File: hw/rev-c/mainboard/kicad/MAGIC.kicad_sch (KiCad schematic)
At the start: 16 parts, among them U7 SN74LVC4245APWR, U8 SN74LVC4245APWR, U9 SN74LVC4245APWR

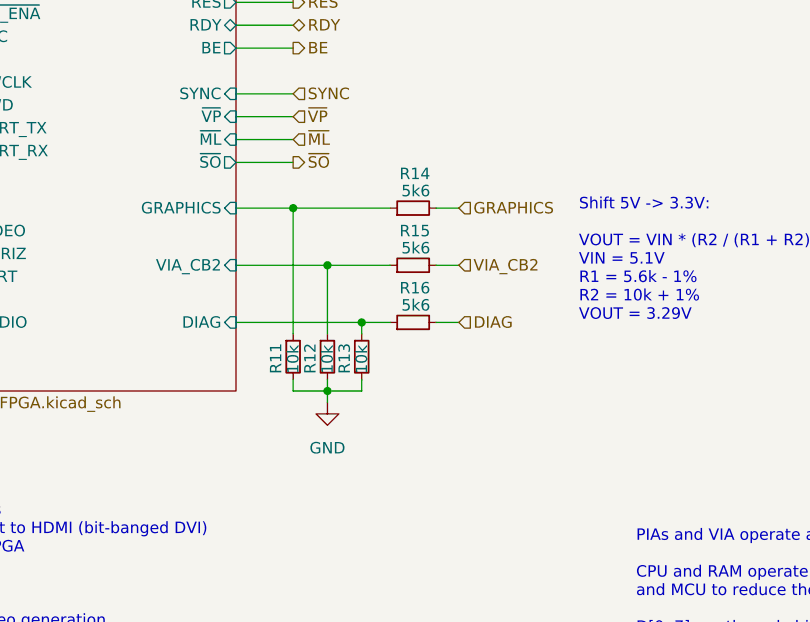
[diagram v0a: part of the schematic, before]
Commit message: hw: fix wire/grid violations in schematic
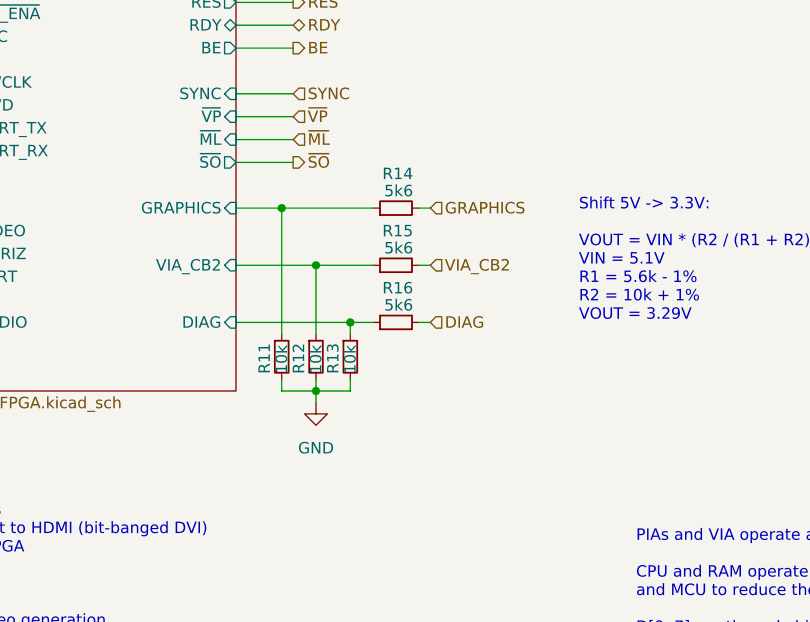
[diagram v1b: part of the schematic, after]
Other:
- moved on the sheet: R11, R12, R13, R14, R15, R16

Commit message: hw: more symbol updates
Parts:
- U7, U8, U9: symbol Mainboard-rescue:SN74LVC8T245-PET -> EconoPET:SN74LVC8T245
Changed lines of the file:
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@@
 	)
 	(symbol
-		(lib_id "Mainboard-rescue:SN74LVC8T245-PET")
+		(lib_id "EconoPET:SN74LVC8T245")
 		(at 220.98 44.45 0)
 		(mirror y)
@@
 	)
 	(symbol
-		(lib_id "Mainboard-rescue:SN74LVC8T245-PET")
+		(lib_id "EconoPET:SN74LVC8T245")
 		(at 223.52 147.32 0)
 		(mirror y)
@@
 	)
 	(symbol
-		(lib_id "Mainboard-rescue:SN74LVC8T245-PET")
+		(lib_id "EconoPET:SN74LVC8T245")
 		(at 222.25 95.25 0)
 		(mirror y)

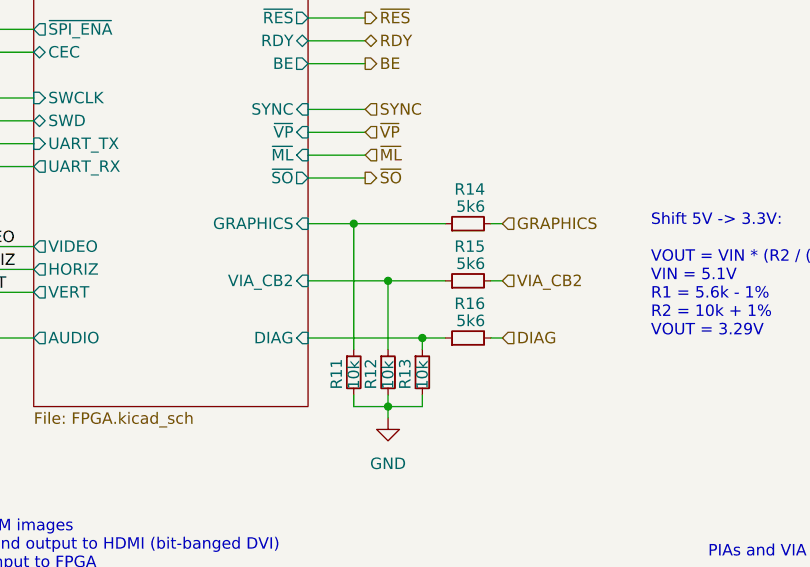
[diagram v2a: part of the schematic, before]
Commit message: hw: renumber reference designators
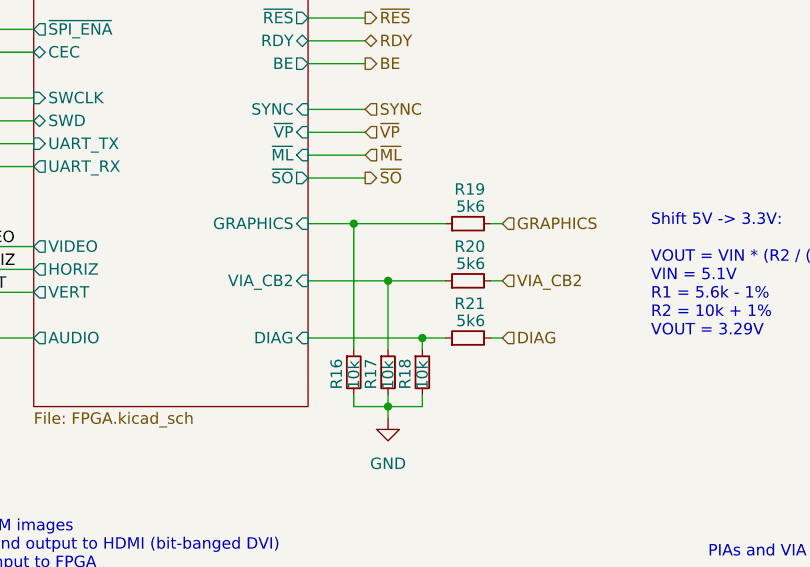
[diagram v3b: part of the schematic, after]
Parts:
- renumbered R11 to R16, R12 to R17, R13 to R18, R14 to R19, R15 to R20, R16 to R21
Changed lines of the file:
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@@
 		(on_board yes)
 		(dnp no)
-		(property "Reference" "#PWR037"
+		(property "Reference" "#PWR038"
 			(at 207.01 74.93 0)
 			(effects
@@
 			(project ""
 				(path "/2eea20e6-112c-411a-b615-885ae773135a/00000000-0000-0000-0000-0000617d6918"
-					(reference "#PWR037")
+					(reference "#PWR038")
 					(unit 1)
 				)
@@
 		(on_board yes)
 		(dnp no)
-		(property "Reference" "#PWR042"
+		(property "Reference" "#PWR043"
 			(at 220.98 68.58 0)
 			(effects
@@
 			(project ""
 				(path "/2eea20e6-112c-411a-b615-885ae773135a/00000000-0000-0000-0000-0000617d6918"
-					(reference "#PWR042")
+					(reference "#PWR043")
 					(unit 1)
 				)
@@
 		(on_board yes)
 		(dnp no)
-		(property "Reference" "#PWR043"
+		(property "Reference" "#PWR044"
 			(at 222.25 119.38 0)
 			(effects
@@
 			(project ""
 				(path "/2eea20e6-112c-411a-b615-885ae773135a/00000000-0000-0000-0000-0000617d6918"
-					(reference "#PWR043")
+					(reference "#PWR044")
 					(unit 1)
 				)
@@
 		(on_board yes)
 		(dnp no)
-		(property "Reference" "#PWR044"
+		(property "Reference" "#PWR045"
 			(at 223.52 171.45 0)
 			(effects
@@
 			(project ""
 				(path "/2eea20e6-112c-411a-b615-885ae773135a/00000000-0000-0000-0000-0000617d6918"
-					(reference "#PWR044")
+					(reference "#PWR045")
 					(unit 1)
 				)
@@
 		(on_board yes)
 		(dnp no)
-		(property "Reference" "#PWR034"
+		(property "Reference" "#PWR035"
 			(at 207.01 24.13 0)
 			(effects
@@
 			(project ""
 				(path "/2eea20e6-112c-411a-b615-885ae773135a/00000000-0000-0000-0000-0000617d6918"
-					(reference "#PWR034")
+					(reference "#PWR035")
 					(unit 1)
 				)
@@
 		(on_board yes)
 		(dnp no)
-		(property "Reference" "#PWR036"
+		(property "Reference" "#PWR037"
 			(at 200.66 34.29 0)
 			(effects
@@
 			(project ""
 				(path "/2eea20e6-112c-411a-b615-885ae773135a/00000000-0000-0000-0000-0000617d6918"
-					(reference "#PWR036")
+					(reference "#PWR037")
 					(unit 1)
 				)
@@
 		(on_board yes)
 		(dnp no)
-		(property "Reference" "#PWR041"
+		(property "Reference" "#PWR042"
 			(at 203.2 137.16 0)
 			(effects
@@
 			(project ""
 				(path "/2eea20e6-112c-411a-b615-885ae773135a/00000000-0000-0000-0000-0000617d6918"
-					(reference "#PWR041")
+					(reference "#PWR042")
 					(unit 1)
 				)
@@
 		(on_board yes)
 		(dnp no)
-		(property "Reference" "#PWR048"
+		(property "Reference" "#PWR049"
 			(at 243.84 137.16 0)
 			(effects
@@
 			(project ""
 				(path "/2eea20e6-112c-411a-b615-885ae773135a/00000000-0000-0000-0000-0000617d6918"
-					(reference "#PWR048")
+					(reference "#PWR049")
 					(unit 1)
 				)
@@
 		(on_board yes)
 		(dnp no)
-		(property "Reference" "#PWR045"
+		(property "Reference" "#PWR046"
 			(at 241.3 34.29 0)
 			(effects
@@
 			(project ""
 				(path "/2eea20e6-112c-411a-b615-885ae773135a/00000000-0000-0000-0000-0000617d6918"
-					(reference "#PWR045")
+					(reference "#PWR046")
 					(unit 1)
 				)
@@
 		(on_board yes)
 		(dnp no)
-		(property "Reference" "#PWR035"
+		(property "Reference" "#PWR036"
 			(at 207.01 31.75 0)
 			(effects
@@
 			(project ""
 				(path "/2eea20e6-112c-411a-b615-885ae773135a/00000000-0000-0000-0000-0000617d6918"
-					(reference "#PWR035")
+					(reference "#PWR036")
 					(unit 1)
 				)
@@
 		(on_board yes)
 		(dnp no)
-		(property "Reference" "R16"
+		(property "Reference" "R21"
 			(at 102.235 113.03 90)
 			(effects
@@
 			(project ""
 				(path "/2eea20e6-112c-411a-b615-885ae773135a/00000000-0000-0000-0000-0000617d6918"
-					(reference "R16")
+					(reference "R21")
 					(unit 1)
 				)
@@
 		(dnp no)
 		(fields_autoplaced yes)
-		(property "Reference" "#PWR050"
+		(property "Reference" "#PWR051"
 			(at 257.81 127 0)
 			(effects
@@
 			(project ""
 				(path "/2eea20e6-112c-411a-b615-885ae773135a/00000000-0000-0000-0000-0000617d6918"
-					(reference "#PWR050")
+					(reference "#PWR051")
 					(unit 1)
 				)
@@
 		(on_board yes)
 		(dnp no)
-		(property "Reference" "R15"
+		(property "Reference" "R20"
 			(at 102.235 106.68 90)
 			(effects
@@
 			(project ""
 				(path "/2eea20e6-112c-411a-b615-885ae773135a/00000000-0000-0000-0000-0000617d6918"
-					(reference "R15")
+					(reference "R20")
 					(unit 1)
 				)
@@
 		(on_board yes)
 		(dnp no)
-		(property "Reference" "R14"
+		(property "Reference" "R19"
 			(at 102.235 100.33 90)
 			(effects
@@
 			(project ""
 				(path "/2eea20e6-112c-411a-b615-885ae773135a/00000000-0000-0000-0000-0000617d6918"
-					(reference "R14")
+					(reference "R19")
 					(unit 1)
 				)
@@
 		(dnp no)
 		(fields_autoplaced yes)
-		(property "Reference" "#PWR033"
+		(property "Reference" "#PWR034"
 			(at 91.44 132.08 0)
 			(effects
@@
 			(project ""
 				(path "/2eea20e6-112c-411a-b615-885ae773135a/00000000-0000-0000-0000-0000617d6918"
-					(reference "#PWR033")
+					(reference "#PWR034")
 					(unit 1)
 				)
@@
 		(on_board yes)
 		(dnp no)
-		(property "Reference" "#PWR047"
+		(property "Reference" "#PWR048"
 			(at 236.22 82.55 0)
 			(effects
@@
 			(project ""
 				(path "/2eea20e6-112c-411a-b615-885ae773135a/00000000-0000-0000-0000-0000617d6918"
-					(reference "#PWR047")
+					(reference "#PWR048")
 					(unit 1)
 				)
@@
 		(on_board yes)
 		(dnp no)
-		(property "Reference" "R13"
+		(property "Reference" "R18"
 			(at 93.345 122.555 90)
 			(effects
@@
 			(project ""
 				(path "/2eea20e6-112c-411a-b615-885ae773135a/00000000-0000-0000-0000-0000617d6918"
-					(reference "R13")
+					(reference "R18")
 					(unit 1)
 				)
@@
 		(dnp no)
 		(fields_autoplaced yes)
-		(property "Reference" "#PWR051"
+		(property "Reference" "#PWR052"
 			(at 262.89 24.13 0)
 			(effects
@@
 			(project ""
 				(path "/2eea20e6-112c-411a-b615-885ae773135a/00000000-0000-0000-0000-0000617d6918"
-					(reference "#PWR051")
+					(reference "#PWR052")
 					(unit 1)
 				)
@@
 		(on_board yes)
 		(dnp no)
-		(property "Reference" "#PWR046"
+		(property "Reference" "#PWR047"
 			(at 236.22 31.75 0)
 			(effects
@@
 			(project ""
 				(path "/2eea20e6-112c-411a-b615-885ae773135a/00000000-0000-0000-0000-0000617d6918"
-					(reference "#PWR046")
+					(reference "#PWR047")
 					(unit 1)
 				)
@@
 		(on_board yes)
 		(dnp no)
-		(property "Reference" "#PWR039"
+		(property "Reference" "#PWR040"
 			(at 207.01 127 0)
 			(effects
@@
 			(project ""
 				(path "/2eea20e6-112c-411a-b615-885ae773135a/00000000-0000-0000-0000-0000617d6918"
-					(reference "#PWR039")
+					(reference "#PWR040")
 					(unit 1)
 				)
@@
 		(on_board yes)
 		(dnp no)
-		(property "Reference" "#PWR040"
+		(property "Reference" "#PWR041"
 			(at 207.01 134.62 0)
 			(effects
@@
 			(project ""
 				(path "/2eea20e6-112c-411a-b615-885ae773135a/00000000-0000-0000-0000-0000617d6918"
-					(reference "#PWR040")
+					(reference "#PWR041")
 					(unit 1)
 				)
@@
 		(on_board yes)
 		(dnp no)
-		(property "Reference" "R11"
+		(property "Reference" "R16"
 			(at 85.725 122.555 90)
 			(effects
@@
 			(project ""
 				(path "/2eea20e6-112c-411a-b615-885ae773135a/00000000-0000-0000-0000-0000617d6918"
-					(reference "R11")
+					(reference "R16")
 					(unit 1)
 				)
@@
 		(on_board yes)
 		(dnp no)
-		(property "Reference" "#PWR038"
+		(property "Reference" "#PWR039"
 			(at 207.01 82.55 0)
 			(effects
@@
 			(project ""
 				(path "/2eea20e6-112c-411a-b615-885ae773135a/00000000-0000-0000-0000-0000617d6918"
-					(reference "#PWR038")
+					(reference "#PWR039")
 					(unit 1)
 				)
@@
 		(on_board yes)
 		(dnp no)
-		(property "Reference" "R12"
+		(property "Reference" "R17"
 			(at 89.535 122.555 90)
 			(effects
@@
 			(project ""
 				(path "/2eea20e6-112c-411a-b615-885ae773135a/00000000-0000-0000-0000-0000617d6918"
-					(reference "R12")
+					(reference "R17")
 					(unit 1)
 				)
@@
 		(on_board yes)
 		(dnp no)
-		(property "Reference" "#PWR049"
+		(property "Reference" "#PWR050"
 			(at 240.03 134.62 0)
 			(effects
@@
 			(project ""
 				(path "/2eea20e6-112c-411a-b615-885ae773135a/00000000-0000-0000-0000-0000617d6918"
-					(reference "#PWR049")
-					(unit 1)
-				)
+					(reference "#PWR050")
+					(unit 1)
+				)
